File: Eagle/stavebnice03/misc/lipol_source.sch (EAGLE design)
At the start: 27 parts

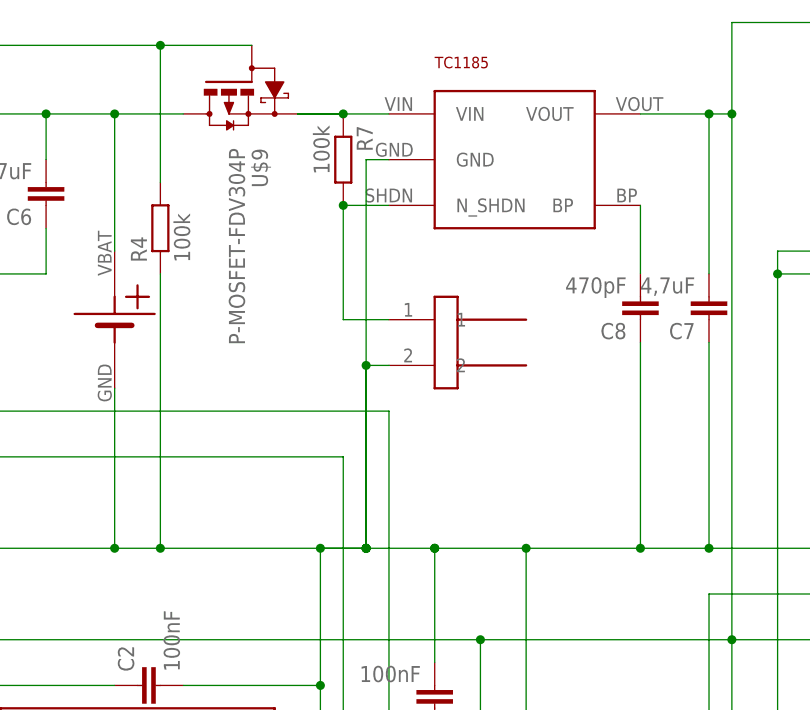
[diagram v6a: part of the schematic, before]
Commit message: element position changed to be able put the bords to boxes + reset button for source board
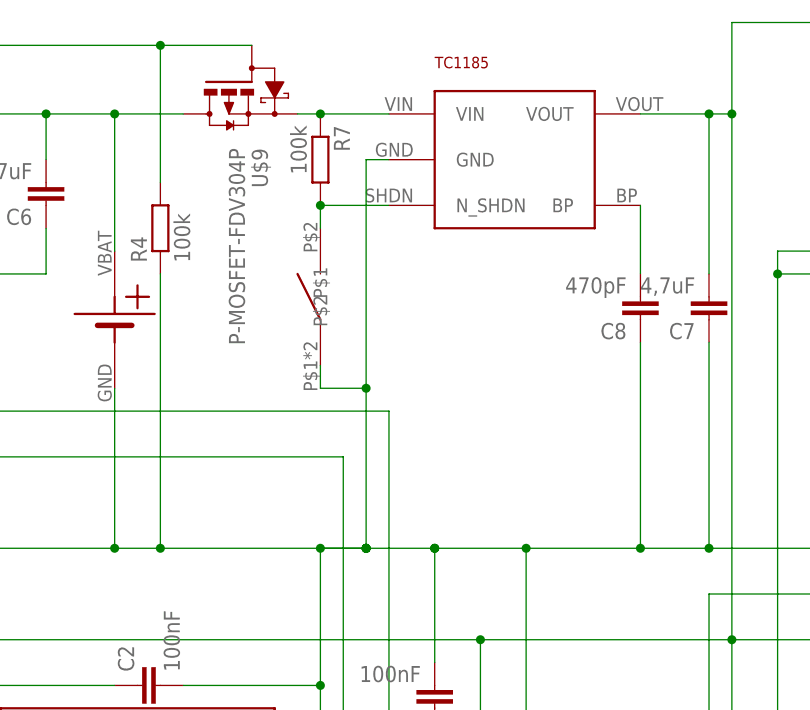
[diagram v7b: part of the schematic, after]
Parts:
- removed U$4: JUMPER2M, !stavebnice03:JUMPER2M
- added U$6: BYTTON-B3U, !stavebnice03:BYTTON-B3U
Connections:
- net GND: now also U$6.P$1; no longer U$4.2
- net N$20: now also U$6.P$2; no longer U$4.1
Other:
- moved on the sheet: R7
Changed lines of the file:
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@@
 <part name="C8" library="resistor" deviceset="C-EU" device="C0603K" value="470pF"/>
 <part name="R7" library="resistor" deviceset="R-EU_" device="R0603" value="100k"/>
-<part name="U$4" library="!stavebnice03" deviceset="JUMPER2M" device=""/>
+<part name="U$6" library="!stavebnice03" deviceset="BYTTON-B3U" device=""/>
 </parts>
 <sheets>
@@
 <instance part="LED2" gate="G$1" x="86.36" y="58.42" rot="R180"/>
 <instance part="C8" gate="G$1" x="200.66" y="144.78" rot="R180"/>
-<instance part="R7" gate="G$1" x="167.64" y="162.56" rot="R270"/>
-<instance part="U$4" gate="G$1" x="180.34" y="142.24"/>
+<instance part="R7" gate="G$1" x="165.1" y="162.56" rot="R270"/>
+<instance part="U$6" gate="G$1" x="165.1" y="147.32" rot="R90"/>
 </instances>
 <busses>
@@
 <pinref part="TC1185" gate="G$1" pin="GND"/>
 <wire x1="172.72" y1="162.56" x2="170.18" y2="162.56" width="0.1524" layer="91"/>
-<wire x1="170.18" y1="162.56" x2="170.18" y2="139.7" width="0.1524" layer="91"/>
+<wire x1="170.18" y1="162.56" x2="170.18" y2="137.16" width="0.1524" layer="91"/>
 <junction x="170.18" y="119.38"/>
 <pinref part="R4" gate="G$1" pin="1"/>
-<wire x1="170.18" y1="139.7" x2="170.18" y2="119.38" width="0.1524" layer="91"/>
 <wire x1="147.32" y1="149.86" x2="147.32" y2="119.38" width="0.1524" layer="91"/>
 <pinref part="C4" gate="G$1" pin="1"/>
@@
 <junction x="170.18" y="119.38"/>
 <junction x="165.1" y="119.38"/>
-<pinref part="U$4" gate="G$1" pin="2"/>
-<wire x1="172.72" y1="139.7" x2="170.18" y2="139.7" width="0.1524" layer="91"/>
-<wire x1="170.18" y1="139.7" x2="170.18" y2="119.38" width="0.1524" layer="91"/>
-<junction x="170.18" y="139.7"/>
+<wire x1="170.18" y1="137.16" x2="170.18" y2="119.38" width="0.1524" layer="91"/>
+<junction x="170.18" y="137.16"/>
+<pinref part="U$6" gate="G$1" pin="P$1"/>
+<wire x1="165.1" y1="139.7" x2="165.1" y2="137.16" width="0.1524" layer="91"/>
+<wire x1="165.1" y1="137.16" x2="170.18" y2="137.16" width="0.1524" layer="91"/>
 </segment>
 </net>
@@
 <pinref part="U$9" gate="G$1" pin="S"/>
 <pinref part="TC1185" gate="G$1" pin="VIN"/>
-<wire x1="162.56" y1="167.64" x2="167.64" y2="167.64" width="0.1524" layer="91"/>
-<wire x1="167.64" y1="167.64" x2="172.72" y2="167.64" width="0.1524" layer="91"/>
-<wire x1="167.64" y1="167.64" x2="162.56" y2="167.64" width="0.1524" layer="91"/>
+<wire x1="165.1" y1="167.64" x2="172.72" y2="167.64" width="0.1524" layer="91"/>
+<wire x1="165.1" y1="167.64" x2="162.56" y2="167.64" width="0.1524" layer="91"/>
 <pinref part="R7" gate="G$1" pin="1"/>
-<junction x="167.64" y="167.64"/>
+<junction x="165.1" y="167.64"/>
 </segment>
 </net>
@@
 <segment>
 <pinref part="TC1185" gate="G$1" pin="N_SHDN"/>
-<wire x1="172.72" y1="157.48" x2="167.64" y2="157.48" width="0.1524" layer="91"/>
-<pinref part="U$4" gate="G$1" pin="1"/>
-<wire x1="167.64" y1="157.48" x2="167.64" y2="144.78" width="0.1524" layer="91"/>
-<wire x1="167.64" y1="144.78" x2="172.72" y2="144.78" width="0.1524" layer="91"/>
+<wire x1="172.72" y1="157.48" x2="165.1" y2="157.48" width="0.1524" layer="91"/>
 <pinref part="R7" gate="G$1" pin="2"/>
-<junction x="167.64" y="157.48"/>
-</segment>
-</net>
+<junction x="165.1" y="157.48"/>
+<pinref part="U$6" gate="G$1" pin="P$2"/>
+<wire x1="165.1" y1="157.48" x2="165.1" y2="154.94" width="0.1524" layer="91"/>
+</segment>
+</net>
